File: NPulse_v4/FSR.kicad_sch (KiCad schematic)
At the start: 15 parts, among them J10 Conn_02x05_Odd_Even, J5 Conn_02x05_Odd_Even, U11 TLV70233_WSON6

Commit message: some modifications on the routing
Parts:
- removed U11: TLV70233_WSON6, Package_SON:Texas_X2SON-4_1x1mm_P0.65mm, symbol Regulator_Linear:TLV70233_WSON6
- added U10: TPS7A0533PDBZ, Package_TO_SOT_SMD:SOT-23, symbol Regulator_Linear:TPS7A0533PDBZ
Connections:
- net +3.3V: now also U10.3 (VI)
- net +5V: now also U10.2 (VO)
- net GND: now also C55.2, C56.2, U10.1 (GND)
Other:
- note added: "Voltage regulator (LDO) TPS7A0533PDBZR MO: 595-TPS7A0533PDBZR"

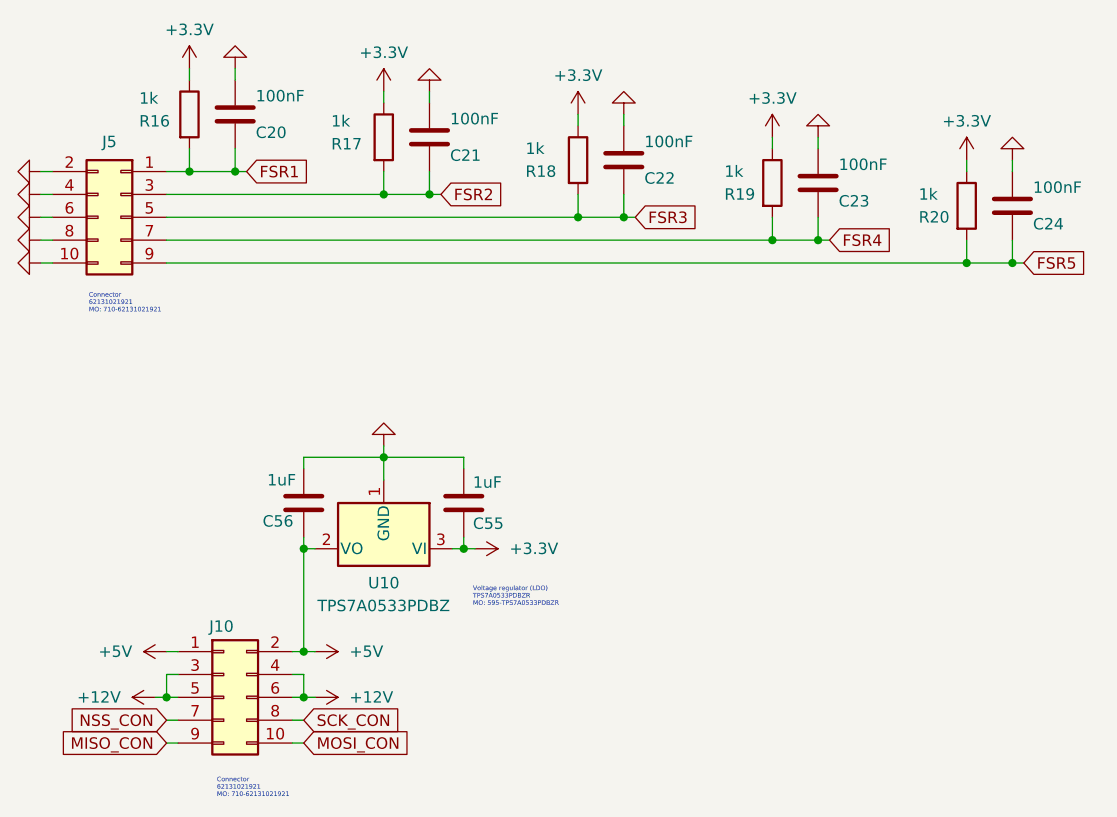
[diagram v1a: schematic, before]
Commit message: Correct LDO schematic and update connectors to through-hole footprints
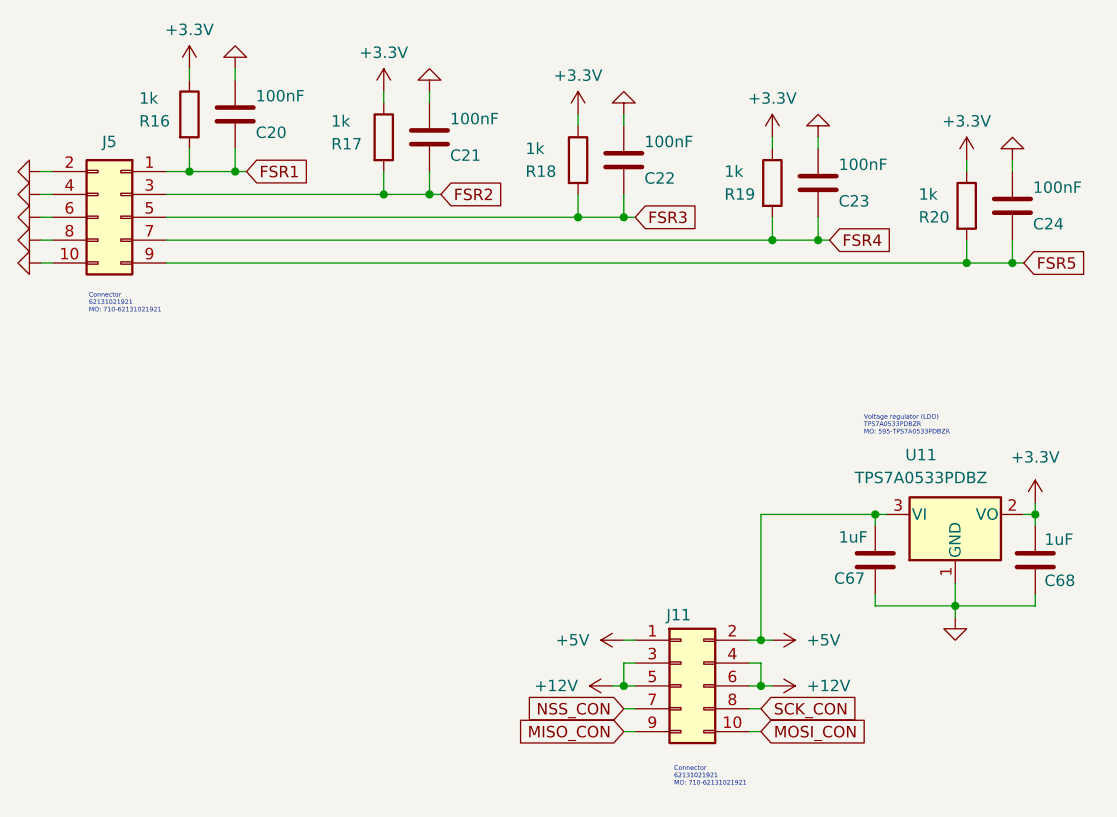
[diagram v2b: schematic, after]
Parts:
- removed C55, C56: 1uF, Capacitor_SMD:C_0402_1005Metric, symbol Device:C
- removed J10: Conn_02x05_Odd_Even, Connector_PinHeader_2.00mm:PinHeader_2x05_P2.00mm_Vertical_SMD, symbol Connector_Generic:Conn_02x05_Odd_Even
- removed U10: TPS7A0533PDBZ, Package_TO_SOT_SMD:SOT-23, symbol Regulator_Linear:TPS7A0533PDBZ
- added C67, C68: 1uF, Capacitor_SMD:C_0402_1005Metric, symbol Device:C
- added J11: Conn_02x05_Odd_Even, Connector_PinHeader_2.00mm:PinHeader_2x05_P2.00mm_Vertical_SMD, symbol Connector_Generic:Conn_02x05_Odd_Even
- added U11: TPS7A0533PDBZ, Package_TO_SOT_SMD:SOT-23, symbol Regulator_Linear:TPS7A0533PDBZ
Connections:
- net +12V: now also J11.3 (Pin_3), J11.4 (Pin_4), J11.5 (Pin_5), J11.6 (Pin_6)
- net +3.3V: now also C68.2, U11.2 (VO)
- net +5V: now also C67.2, J11.1 (Pin_1), J11.2 (Pin_2), U11.3 (VI)
- net GND: now also C67.1, C68.1, U11.1 (GND)
- net MISO_CON: now also J11.9 (Pin_9)
- net MOSI_CON: now also J11.10 (Pin_10)
- net NSS_CON: now also J11.7 (Pin_7)
- net SCK_CON: now also J11.8 (Pin_8)
